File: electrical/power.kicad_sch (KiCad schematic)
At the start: 43 parts

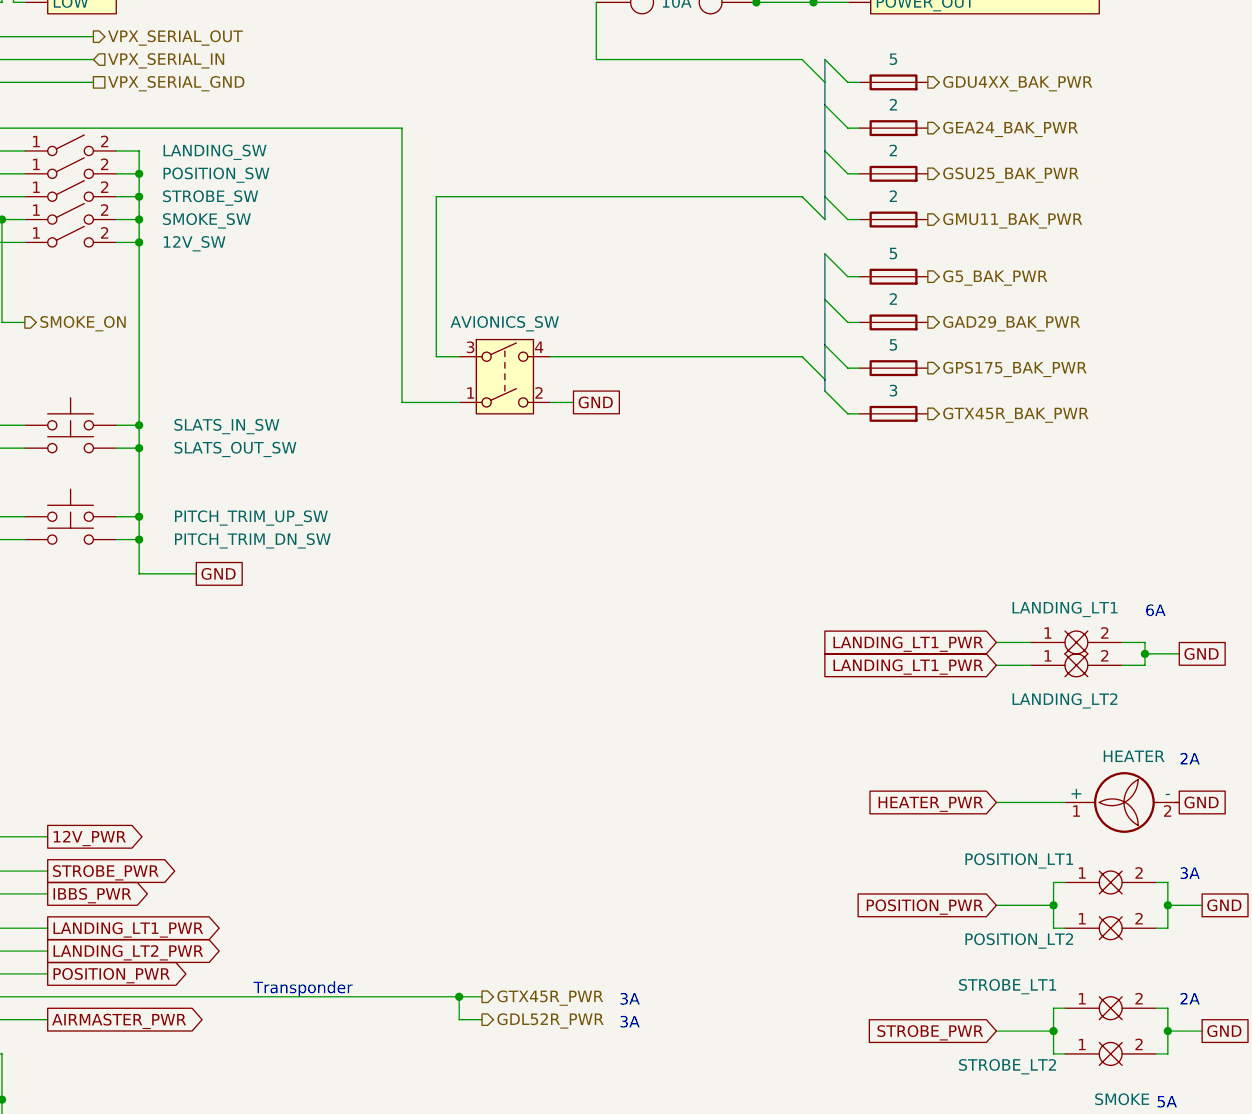
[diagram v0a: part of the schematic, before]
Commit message: Removed lights & trim/flaps power coming out of power overview. Renamed position to nav.
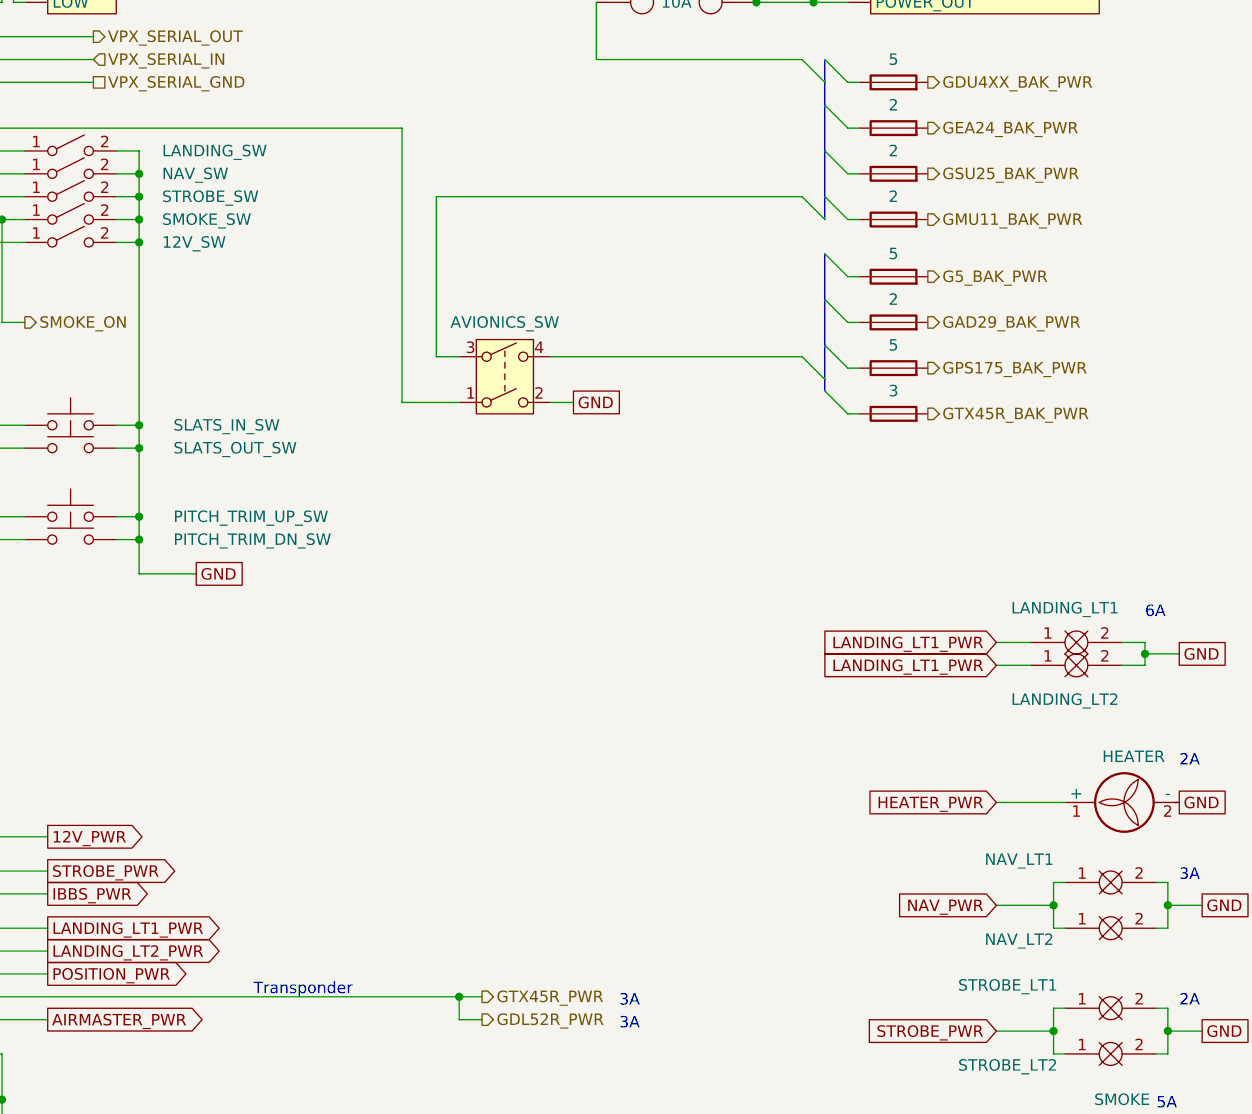
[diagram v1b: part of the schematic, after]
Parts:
- renumbered POSITION_LT1 to NAV_LT1, POSITION_LT2 to NAV_LT2, POSITION_SW to NAV_SW
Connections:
- net POSITION_PWR: no longer NAV_LT1.1, NAV_LT2.1
- new net NAV_PWR: NAV_LT1.1, NAV_LT2.1
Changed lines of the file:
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@@
     )
   )
-  (global_label "POSITION_PWR" (shape input) (at 167.64 160.02 180) (fields_autoplaced)
+  (global_label "NAV_PWR" (shape input) (at 167.64 160.02 180) (fields_autoplaced)
     (effects (font (size 1.27 1.27)) (justify right))
-    (property "Intersheetrefs" "${INTERSHEET_REFS}" (at 151.0476 160.02 0)
+    (property "Intersheetrefs" "${INTERSHEET_REFS}" (at 156.1881 160.02 0)
       (effects (font (size 1.27 1.27)) (justify right) hide)
     )
@@
   (symbol (lib_id "FlyerX:Bulb") (at 179.07 156.21 0) (unit 1)
     (in_bom yes) (on_board yes) (dnp no)
-    (property "Reference" "POSITION_LT1" (at 170.18 154.94 0)
+    (property "Reference" "NAV_LT1" (at 170.18 154.94 0)
       (effects (font (size 1.27 1.27)))
     )
@@
       (project "electrical"
         (path "/e8ec215a-dbe2-4eba-a577-e50a0a128049/2852c073-fbc9-4469-a6bf-ba3e911c7f5a"
-          (reference "POSITION_LT1") (unit 1)
+          (reference "NAV_LT1") (unit 1)
         )
       )
@@
   (symbol (lib_id "FlyerX:Bulb") (at 179.07 161.29 0) (unit 1)
     (in_bom yes) (on_board yes) (dnp no)
-    (property "Reference" "POSITION_LT2" (at 170.18 163.83 0)
+    (property "Reference" "NAV_LT2" (at 170.18 163.83 0)
       (effects (font (size 1.27 1.27)))
     )
@@
       (project "electrical"
         (path "/e8ec215a-dbe2-4eba-a577-e50a0a128049/2852c073-fbc9-4469-a6bf-ba3e911c7f5a"
-          (reference "POSITION_LT2") (unit 1)
+          (reference "NAV_LT2") (unit 1)
         )
       )
@@
   (symbol (lib_id "Switch:SW_SPST") (at 64.77 78.74 0) (unit 1)
     (in_bom yes) (on_board yes) (dnp no)
-    (property "Reference" "POSITION_SW" (at 74.93 78.74 0)
+    (property "Reference" "NAV_SW" (at 74.93 78.74 0)
       (effects (font (size 1.27 1.27)) (justify left))
     )
@@
       (project "electrical"
         (path "/e8ec215a-dbe2-4eba-a577-e50a0a128049/2852c073-fbc9-4469-a6bf-ba3e911c7f5a"
-          (reference "POSITION_SW") (unit 1)
-        )
-      )
+          (reference "NAV_SW") (unit 1)
+        )
+      )

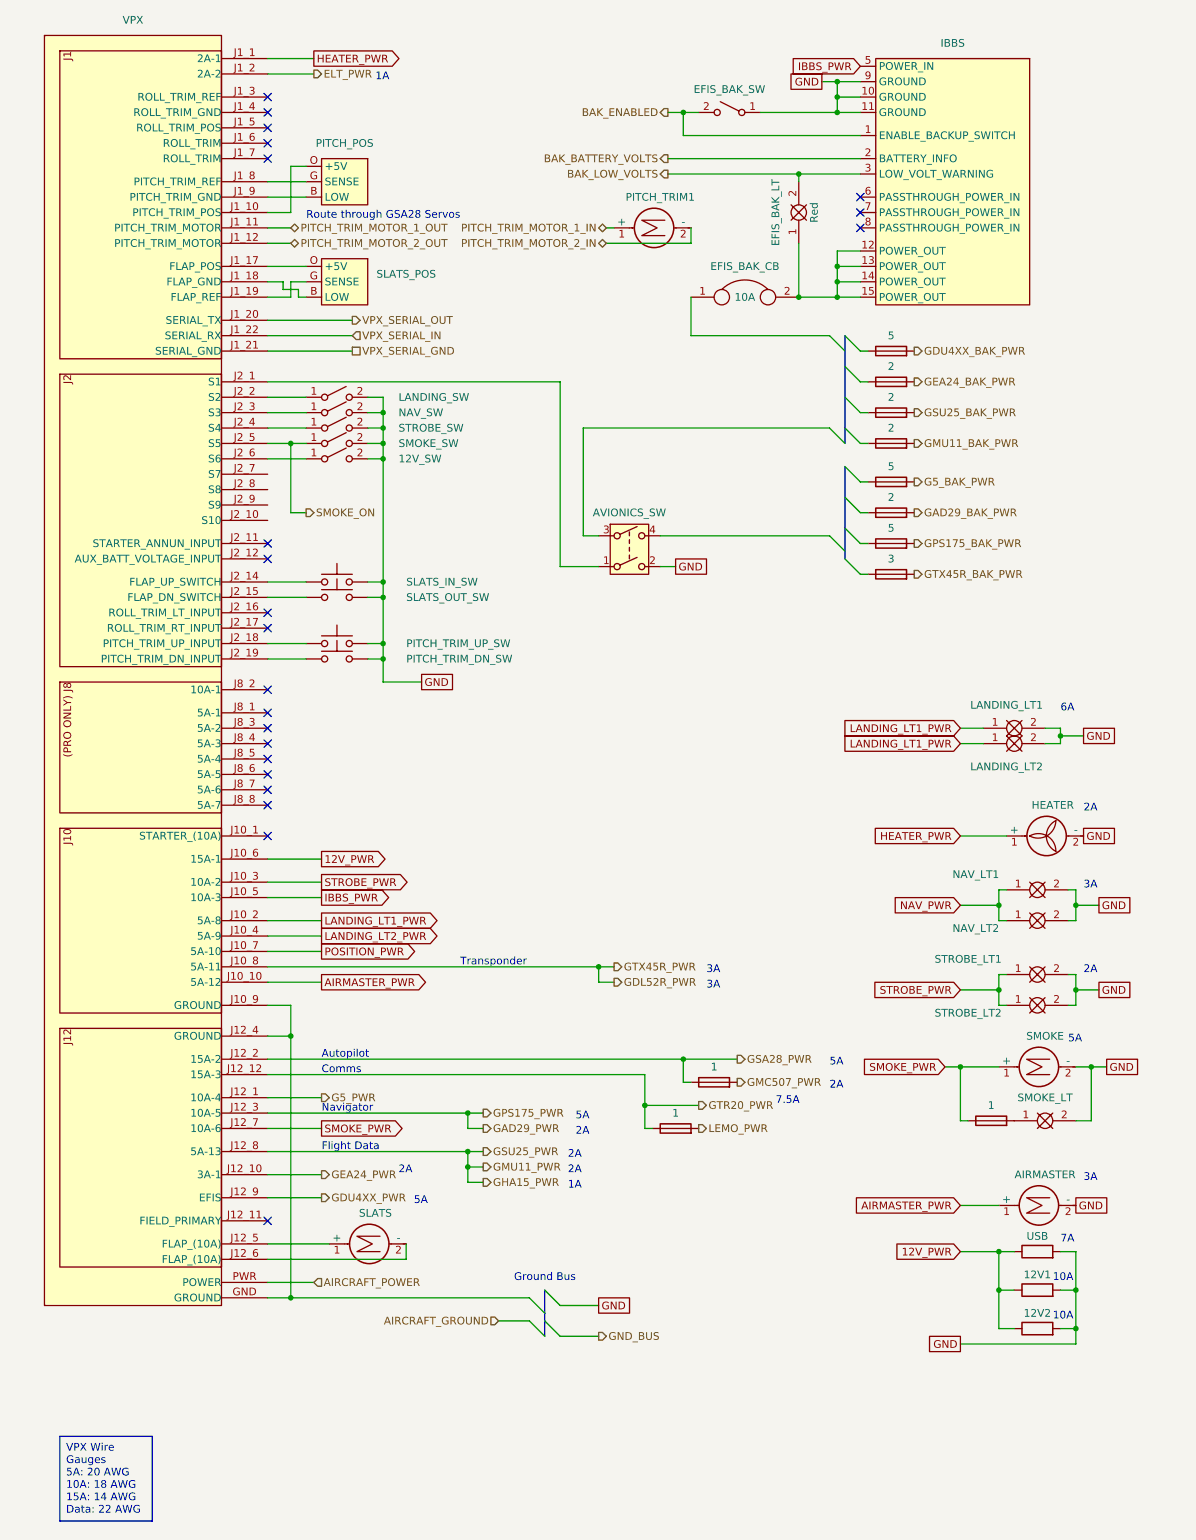
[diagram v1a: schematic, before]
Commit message: Switch Slats to use Roll and put Flaps on Flaps.
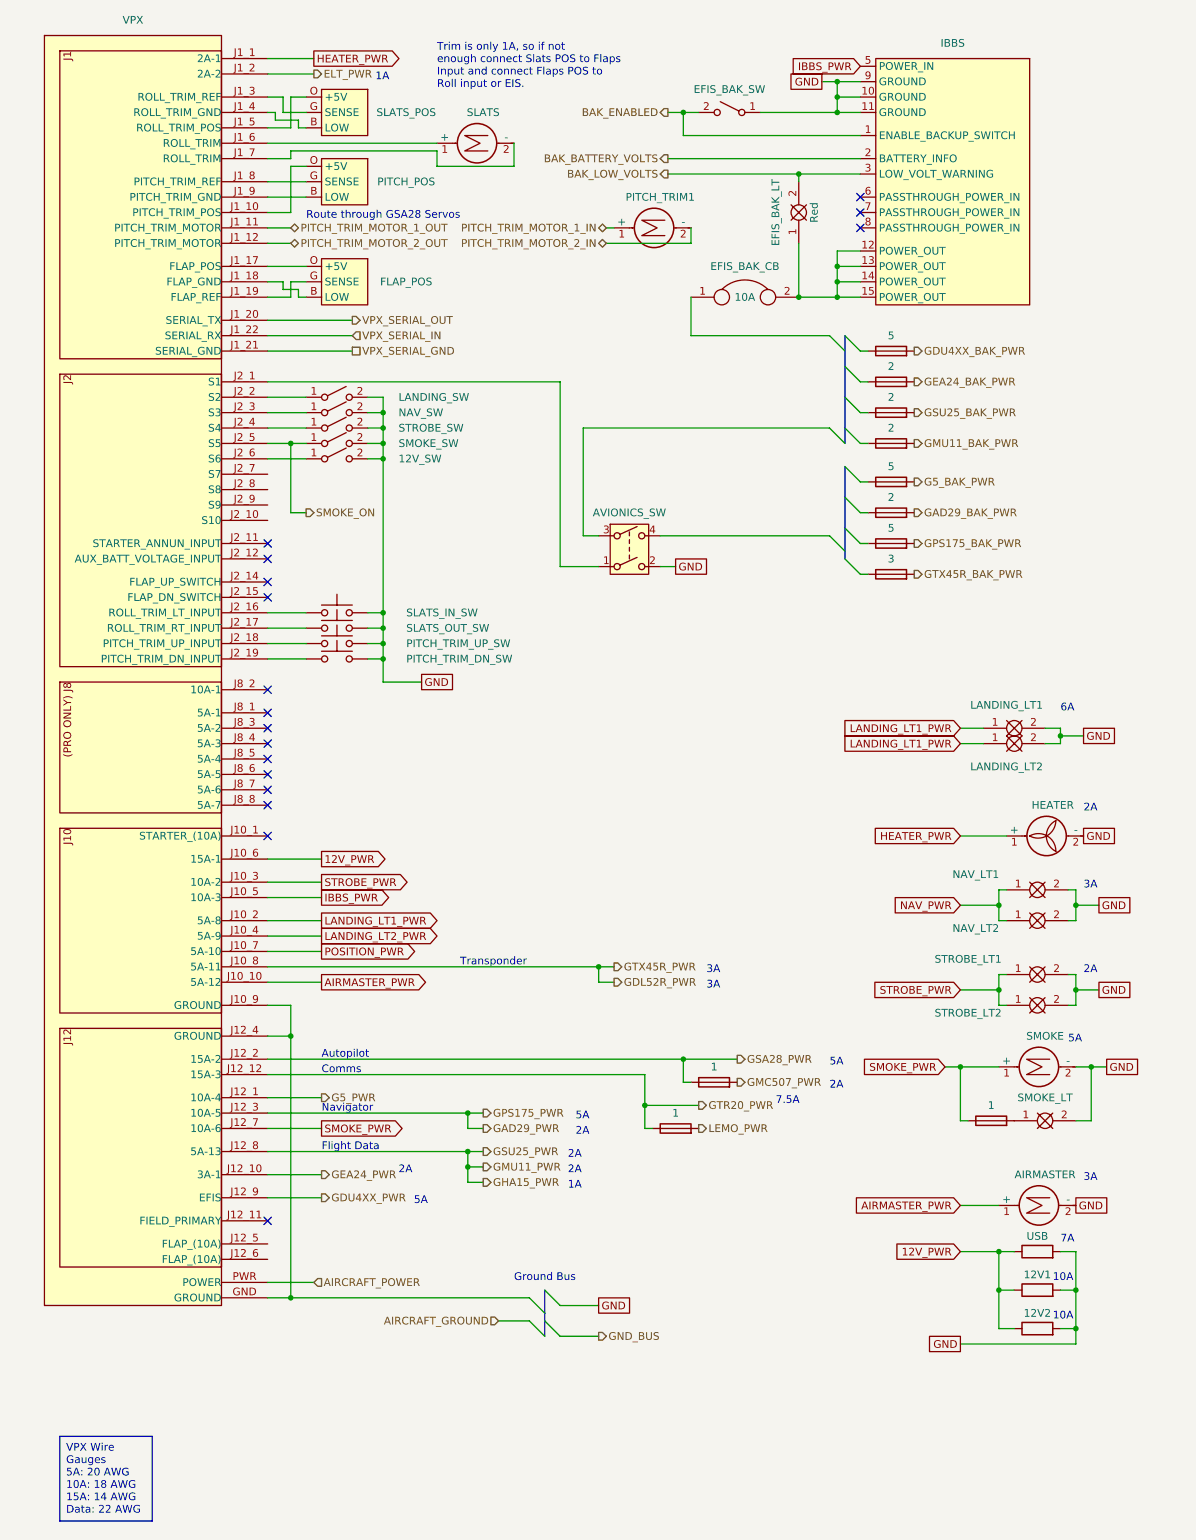
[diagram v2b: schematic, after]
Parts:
- added SLATS_POS: ~, symbol flyerx:Ray_Allen_POS-12
- renumbered SLATS_POS to FLAP_POS
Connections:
- net at VPX.J12_5 (FLAP_(10A)): no longer SLATS.1 (+)
- net at VPX.J12_6 (FLAP_(10A)): no longer SLATS.2 (-)
- net at VPX.J1_3 (ROLL_TRIM_REF): now also SLATS_POS.G (SENSE)
- net at VPX.J1_4 (ROLL_TRIM_GND): now also SLATS_POS.B (LOW)
- net at VPX.J1_5 (ROLL_TRIM_POS): now also SLATS_POS.O (+5V)
- net at VPX.J1_6 (ROLL_TRIM): now also SLATS.1 (+)
- net at VPX.J1_7 (ROLL_TRIM): now also SLATS.2 (-)
- net at VPX.J2_14 (FLAP_UP_SWITCH): no longer SLATS_IN_SW.1
- net at VPX.J2_15 (FLAP_DN_SWITCH): no longer SLATS_OUT_SW.1
- net at VPX.J2_16 (ROLL_TRIM_LT_INPUT): now also SLATS_IN_SW.1
- net at VPX.J2_17 (ROLL_TRIM_RT_INPUT): now also SLATS_OUT_SW.1
- no-connect marks 22 -> 17
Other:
- note added: "Trim is only 1A, so if not enough connect Slats POS to Flaps Input and connect Flaps POS to Roll input or EIS."
- moved on the sheet: SLATS_IN_SW, SLATS_OUT_SW

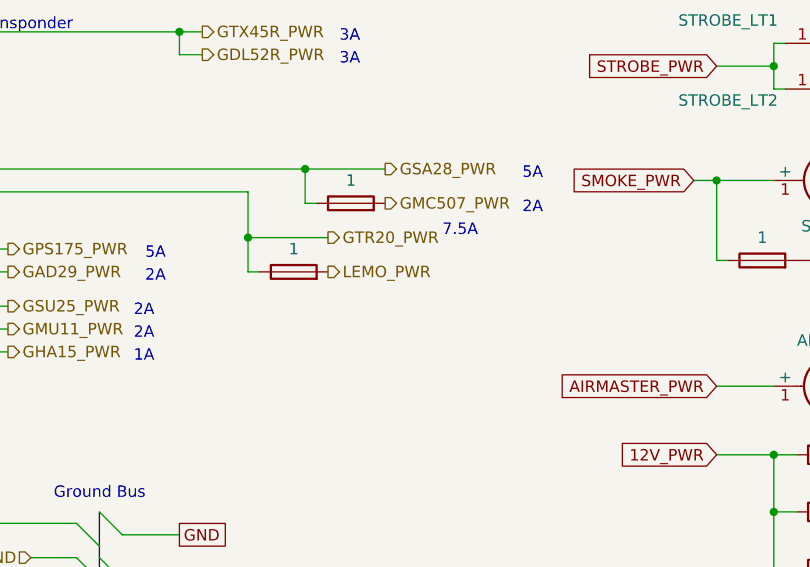
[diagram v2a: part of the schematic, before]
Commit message: Added bluetooth
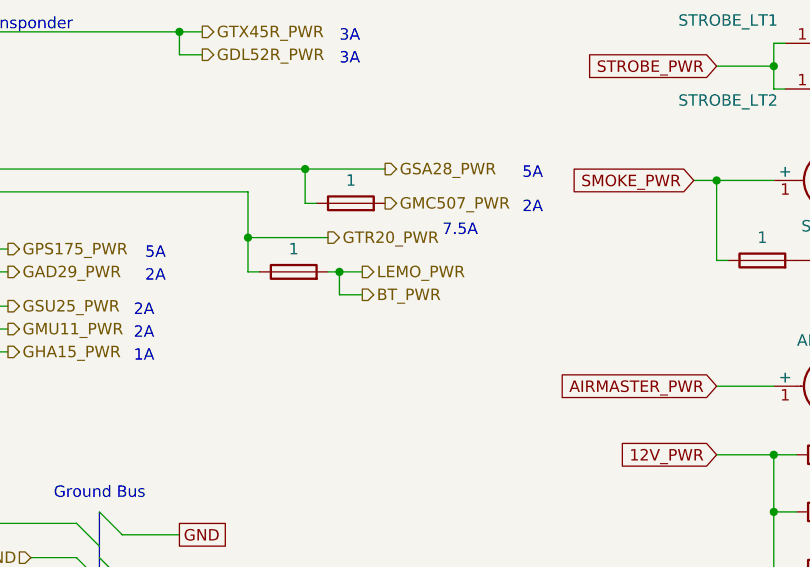
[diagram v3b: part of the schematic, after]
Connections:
- net LEMO_PWR renamed BT_PWR
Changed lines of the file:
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@@
   (junction (at 72.39 81.28) (diameter 0) (color 0 0 0 0)
+  )
+  (junction (at 125.73 196.85) (diameter 0) (color 0 0 0 0)
   )
   (junction (at 186.69 160.02) (diameter 0) (color 0 0 0 0)
@@
     (stroke (width 0) (type default))
   )
+  (wire (pts (xy 125.73 196.85) (xy 124.46 196.85))
+    (stroke (width 0) (type default))
+  )
   (wire (pts (xy 88.9 196.85) (xy 86.36 196.85))
     (stroke (width 0) (type default))
@@
     (stroke (width 0) (type default))
   )
+  (wire (pts (xy 125.73 199.39) (xy 125.73 196.85))
+    (stroke (width 0) (type default))
+  )
   (wire (pts (xy 101.6 226.06) (xy 107.95 226.06))
     (stroke (width 0) (type default))
@@
     (stroke (width 0) (type default))
   )
+  (wire (pts (xy 128.27 199.39) (xy 125.73 199.39))
+    (stroke (width 0) (type default))
+  )
   (wire (pts (xy 115.57 187.96) (xy 115.57 193.04))
     (stroke (width 0) (type default))
@@
   )
   (wire (pts (xy 186.69 162.56) (xy 186.69 160.02))
+    (stroke (width 0) (type default))
+  )
+  (wire (pts (xy 128.27 196.85) (xy 125.73 196.85))
     (stroke (width 0) (type default))
   )
@@
     )
   )
+  (hierarchical_label "BT_PWR" (shape output) (at 128.27 199.39 0) (fields_autoplaced)
+    (effects (font (size 1.27 1.27)) (justify left))
+  )
   (hierarchical_label "GSA28_PWR" (shape output) (at 130.81 185.42 0) (fields_autoplaced)
     (effects (font (size 1.27 1.27)) (justify left))
@@
     (effects (font (size 1.27 1.27)) (justify left))
   )
-  (hierarchical_label "LEMO_PWR" (shape output) (at 124.46 196.85 0) (fields_autoplaced)
-    (effects (font (size 1.27 1.27)) (justify left))
-  )
+  (hierarchical_label "LEMO_PWR" (shape output) (at 128.27 196.85 0) (fields_autoplaced)
+    (effects (font (size 1.27 1.27)) (justify left))
+  )
